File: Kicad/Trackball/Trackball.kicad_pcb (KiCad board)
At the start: 2 copper layers, 231.1 x 140.2 mm, 66 parts, among them J1 Battery, J10 Conn_01x04_Female, J11 Conn_01x04_Female, J12 Conn_01x04_Female, J13 Conn_01x04_Female, J14 Conn_01x04_Female, J15 Conn_01x04_Female, J17 Conn_01x04_Female, J18 Conn_01x03_Pin, J19 Conn_01x03_Pin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

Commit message: B5: Replaced switches, added soldering pad switches to configure the button switch orientation, added break-outs to detach the flaps over the switches.
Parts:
- added JP1: SolderJumper_3_Open, Jumper:SolderJumper-3_P1.3mm_Open_RoundedPad1.0x1.5mm, B.Cu at (116.2, 42.8)
- added JP2: SolderJumper_3_Open, Jumper:SolderJumper-3_P1.3mm_Open_RoundedPad1.0x1.5mm, B.Cu at (217.4, 36.5)
- added JP3: SolderJumper_3_Open, Jumper:SolderJumper-3_P1.3mm_Open_RoundedPad1.0x1.5mm, B.Cu at (235.5, 44.5)
- added JP4: SolderJumper_3_Open, Jumper:SolderJumper-3_P1.3mm_Open_RoundedPad1.0x1.5mm, B.Cu at (115.9, 120.5)
- added JP5: SolderJumper_3_Open, Jumper:SolderJumper-3_P1.3mm_Open_RoundedPad1.0x1.5mm, B.Cu at (217.2, 126.7)
- added JP6: SolderJumper_3_Open, Jumper:SolderJumper-3_P1.3mm_Open_RoundedPad1.0x1.5mm, B.Cu at (234.7, 118.7)
- J10, J13: value Conn_01x04_Female -> Female
- J2, J3: value Conn_01x04_Male -> Male
- MX1, MX2, MX3, MX4, MX5, MX6: value MX-NoLED -> SW_SPDT
- moved H18 20.7 mm to (45.3, 52.9)
- moved H24 20.6 mm to (150.5, 52.9)
- moved H25 20.6 mm to (132.4, 52.9)
- moved MX1 20.0 mm to (112.7, 47.9)
- moved BT_RESET1 20.0 mm to (147.7, 65.1)
- moved BT_SELECT1 20.0 mm to (154.4, 65.1)
- moved H1 20.0 mm to (184.7, 81.6)
- moved H11 20.0 mm to (121.4, 99.6)
- moved H12 20.0 mm to (140.4, 68.6)
- moved H14 20.0 mm to (140.4, 94.6)
- moved H15 20.0 mm to (209.4, 99.6)
- moved H16 20.0 mm to (72.4, 68.6)
- moved H17 20.0 mm to (72.4, 94.6)
- moved H2 20.0 mm to (49.9, 71.6)
- moved H3 20.0 mm to (49.9, 91.6)
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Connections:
- MX1 pad 1: Button1 -> Net-(JP1-A)
- MX1 pad 3: (no net) -> Net-(JP1-B)
- MX2 pad 1: GNDA -> Net-(JP2-A)
- MX2 pad 2: Net-(J10-Pin_2) -> GNDA
- MX2 pad 3: (no net) -> Net-(JP2-B)
- MX3 pad 1: GNDA -> Net-(JP3-A)
- MX3 pad 2: Net-(J10-Pin_3) -> GNDA
- MX3 pad 3: (no net) -> Net-(JP3-B)
- MX4 pad 1: GND -> Net-(JP4-A)
- MX4 pad 2: Button4 -> GND
- MX4 pad 3: (no net) -> Net-(JP4-B)
- MX5 pad 1: Net-(J13-Pin_2) -> Net-(JP5-A)
- MX5 pad 3: (no net) -> Net-(JP5-B)
- MX6 pad 1: Net-(J13-Pin_3) -> Net-(JP6-A)
- MX6 pad 3: (no net) -> Net-(JP6-B)
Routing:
- net GND: track 25.1 -> 4.10 mm, vias 33 -> 32
- net Button4: track 76.8 -> 69.2 mm, vias 1 -> 2
- net Net-(J10-Pin_3): track 47.1 -> 40.8 mm
- net Net-(JP6-B): track 0.00 -> 5.32 mm
- net Net-(JP6-A): track 0.00 -> 5.32 mm
- net Net-(JP1-B): track 0.00 -> 5.20 mm
- net Net-(JP1-A): track 0.00 -> 5.20 mm
- net Net-(JP4-A): track 0.00 -> 5.17 mm, vias 0 -> 1
- net Net-(JP5-A): track 0.00 -> 5.13 mm
- net Net-(JP5-B): track 0.00 -> 5.13 mm
- net Net-(JP2-A): track 0.00 -> 5.01 mm
- net Net-(JP2-B): track 0.00 -> 5.01 mm
- net Net-(JP4-B): track 0.00 -> 5.00 mm
- net Net-(JP3-B): track 0.00 -> 4.98 mm
- net Net-(JP3-A): track 0.00 -> 4.98 mm
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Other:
- board size 231.1 x 140.2 mm -> 231.1 x 160.2 mm
- board text added: "ThumbsUp! Trackball v5"
- board text added: "u/ak66666 2025-09-26"
- board text added: "u/ak66666 ThumbsUp! Trackball v5 2025-09-26"
- board text removed: "ThumbsUp! Trackball v3 rev.2"
- board text removed: "u/ak66666 2025-09-23"
- board text removed: "u/ak66666 ThumbsUp! Trackball v3 rev.2 2025-09-24"

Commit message: B5: Tried to upload to JLC, corrected the labels, error-checked.
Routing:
- net Net-(JP4-A): vias 1 -> 0
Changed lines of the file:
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@@
 	)
 	(gr_rect
-		(start 215.15 69.6)
-		(end 225.4 93.85)
+		(start 217.65 68.1)
+		(end 225.4 96.35)
 		(stroke
 			(width 0.12)
@@
 		(layer "Edge.Cuts")
 	)
+	(gr_text "BATTERY \nON-OFF"
+		(at 169.525 81.35 90)
+		(layer "F.Mask" knockout)
+		(effects
+			(font
+				(size 1.5 1.5)
+				(thickness 0.3)
+				(bold yes)
+			)
+			(justify bottom)
+		)
+	)
 	(gr_text "u/ak66666\nThumbsUp! Trackball v5\n2025-09-26"
 		(at 224.9 82.35 90)
@@
 		)
 	)
-	(gr_text "BATTERY \nON-OFF"
-		(at 169.525 81.35 90)
-		(layer "Dwgs.User" knockout)
-		(effects
-			(font
-				(size 1.5 1.5)
-				(thickness 0.3)
-				(bold yes)
-			)
-			(justify bottom)
-		)
-	)
 	(segment
 		(start 116.1 51.1)
@@
 		(net 61)
 	)
-	(via
-		(at 112.747 115.382)
-		(size 0.8)
-		(drill 0.4)
-		(layers "F.Cu" "B.Cu")
-		(net 62)
-	)
 	(segment
 		(start 112.747 116.097)
@@
 		(min_thickness 0.254)
 		(filled_areas_thickness no)
-		(fill
+		(fill yes
 			(thermal_gap 0.508)
 			(thermal_bridge_width 0.508)
@@
 		(min_thickness 0.254)
 		(filled_areas_thickness no)
-		(fill
+		(fill yes
 			(mode hatch)
 			(thermal_gap 0.508)
@@
 		(min_thickness 0.25)
 		(filled_areas_thickness no)
-		(fill
+		(fill yes
 			(mode hatch)
 			(thermal_gap 0.5)
@@
 		(min_thickness 0.25)
 		(filled_areas_thickness no)
-		(fill
+		(fill yes
 			(thermal_gap 0.5)
 			(thermal_bridge_width 0.5)
@@
 		(min_thickness 0.25)
 		(filled_areas_thickness no)
-		(fill
+		(fill yes
 			(mode hatch)
 			(thermal_gap 0.5)
@@
 		(min_thickness 0.25)
 		(filled_areas_thickness no)
-		(fill
+		(fill yes
 			(mode hatch)
 			(thermal_gap 0.5)

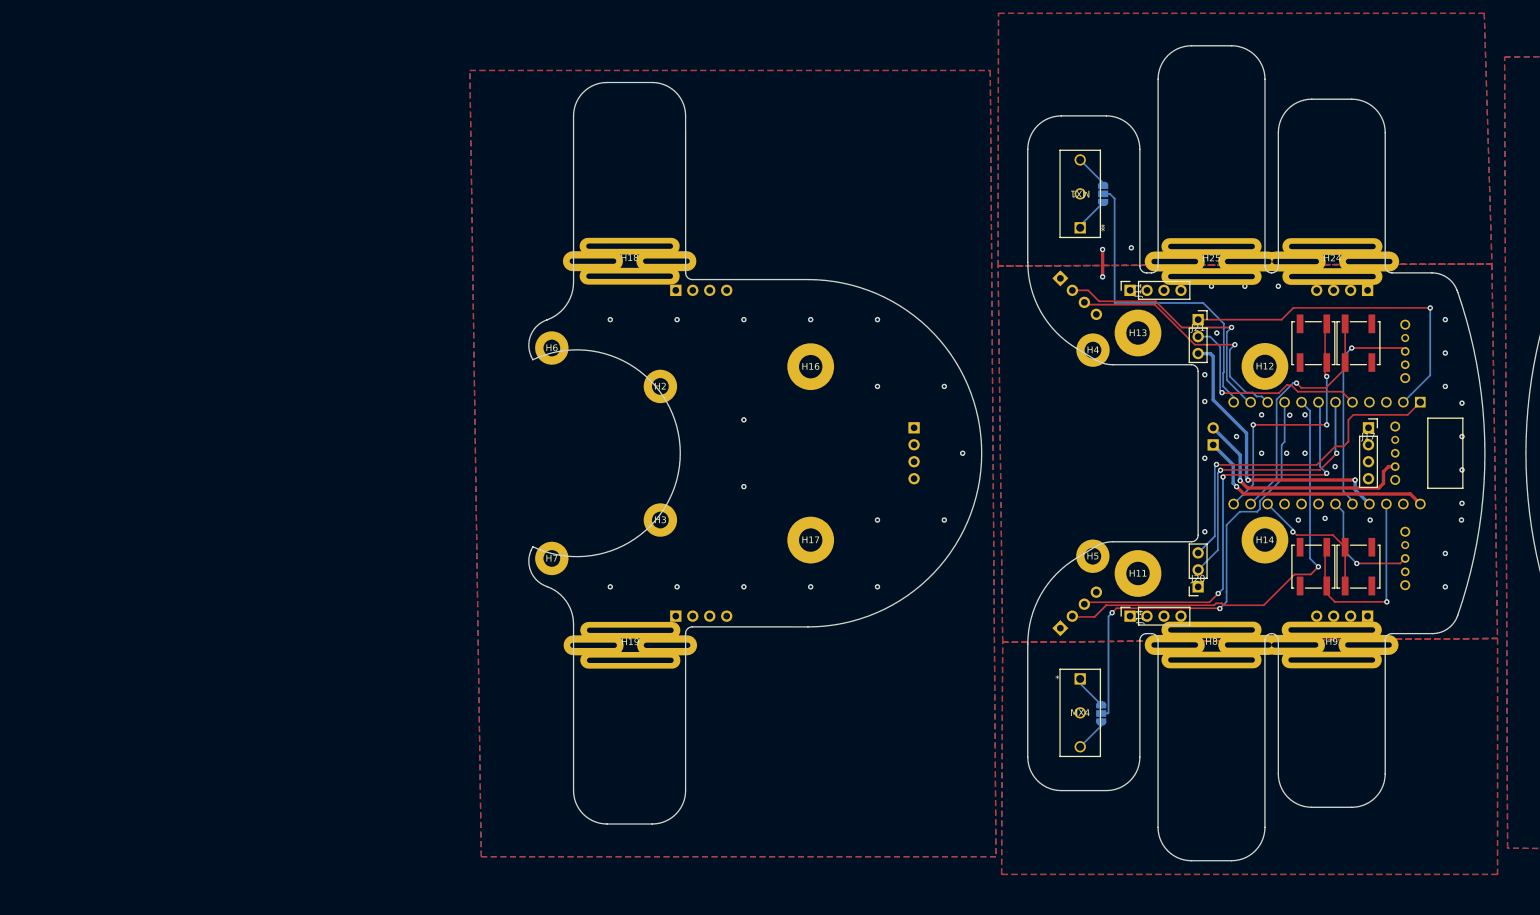
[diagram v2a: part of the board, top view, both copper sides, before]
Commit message: B5: Separated key flaps into a separate panel. Added photos of rev.1 device.
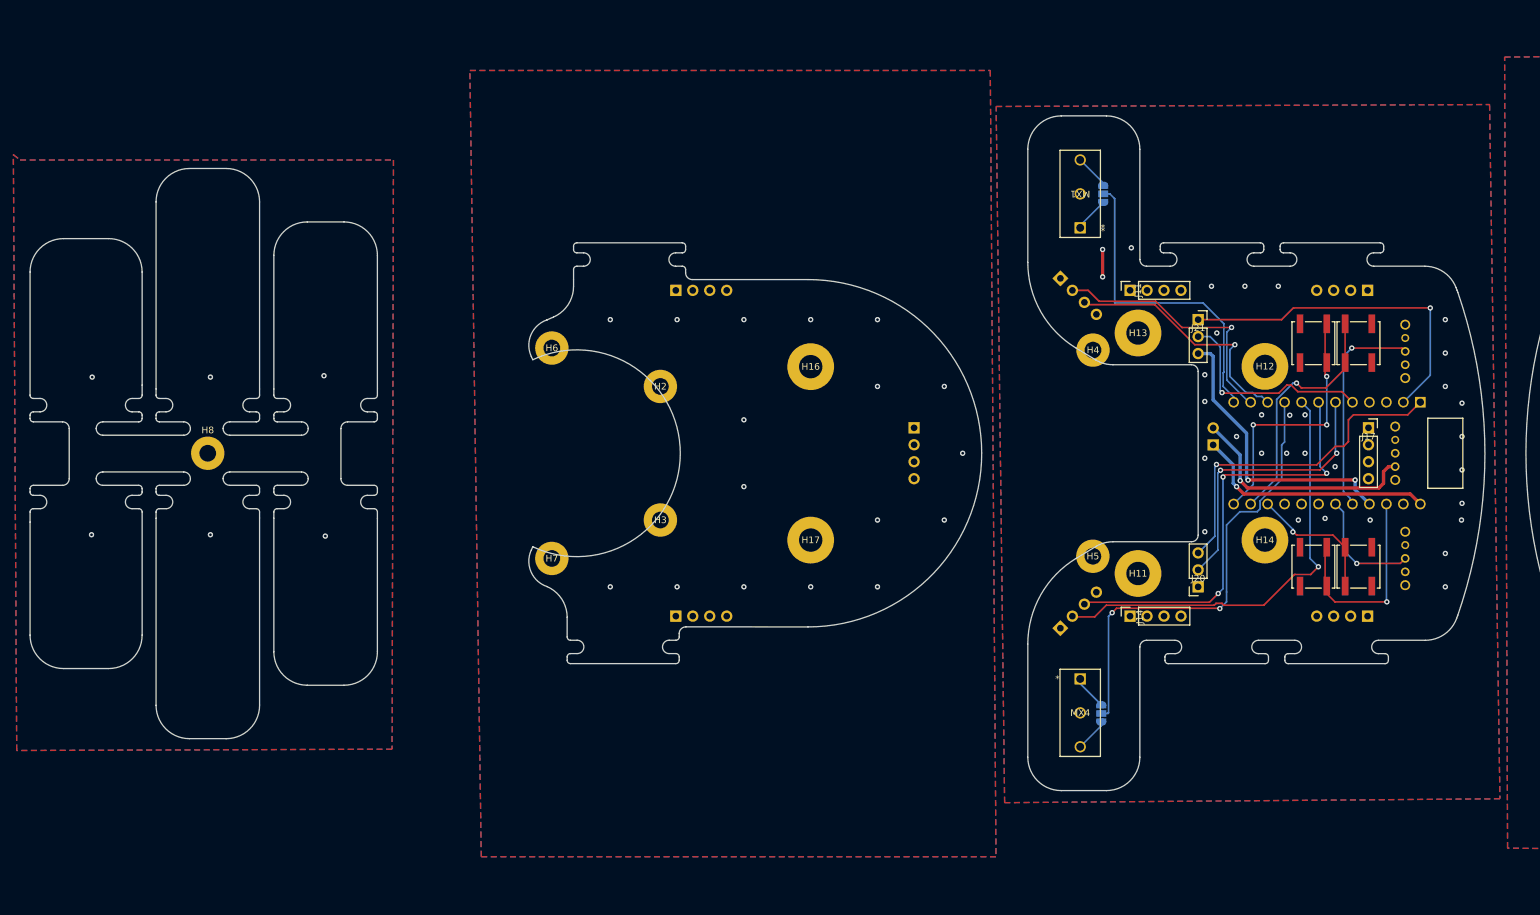
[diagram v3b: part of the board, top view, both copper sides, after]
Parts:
- removed H18, H19, H24, H25, H9: MountingHole_Pad, ButtonLevers:ButtonLever_HingeSlot
- H8: footprint ButtonLevers:ButtonLever_HingeSlot -> MountingHole:MountingHole_2.5mm_Pad
- moved H8 153.0 mm to (-17.9, 81.6)
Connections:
- H8 pad 1: GND -> GND_F
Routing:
- net GND_F: vias 0 -> 6
- added copper zone on B.Cu, net GND_F
- added copper zone on F.Cu, net GND_F
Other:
- board size 231.1 x 160.2 mm -> 305.8 x 154.1 mm
- board text added: "L1"
- board text added: "L2"
- board text added: "L3"
- board text added: "R1"
- board text added: "R2"
- board text added: "R3"

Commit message: B5: Fixed the validation errors, ready to regenerate Gerbers
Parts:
- moved J11 3.00 mm to (117.2, 57.2)
- moved J14 3.00 mm to (117.2, 106.0)
- moved J7 3.00 mm to (49.2, 57.2)
- moved J8 3.00 mm to (49.2, 106.0)
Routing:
- net Button4: track 69.2 -> 66.1 mm
- net Button1: track 47.7 -> 46.7 mm
- net Button5: track 65.5 -> 66.3 mm
- net GND: vias 32 -> 33
